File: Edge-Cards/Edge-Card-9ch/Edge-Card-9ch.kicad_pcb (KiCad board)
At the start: 2 copper layers, 20.7 x 8.8 mm, 1 part

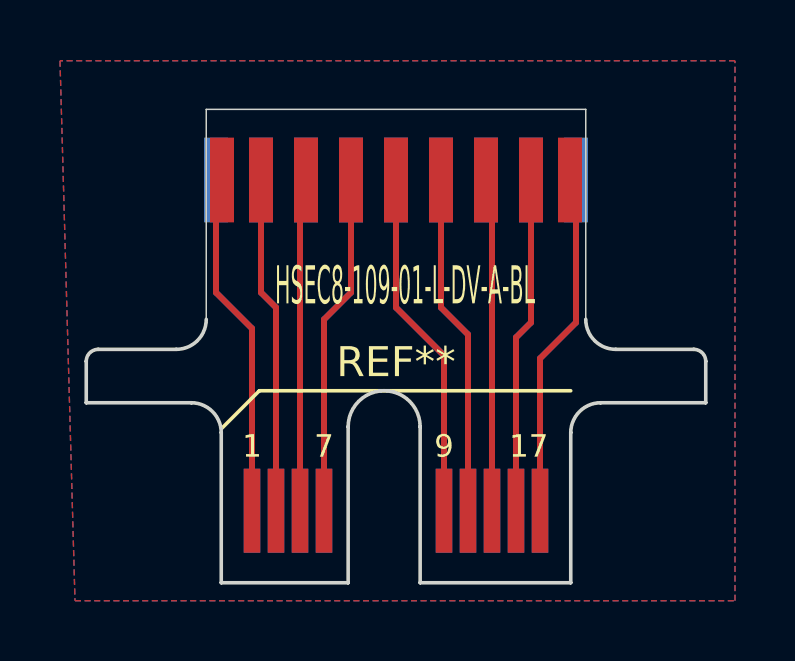
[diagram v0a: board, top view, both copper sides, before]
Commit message: Edge Card 9ch v2 + 9ch latch IV board v2 +
Updated Edge Card 9ch to v2 with expanded pads, and fixed 9ch latch IV board to reroute one trace around a hole
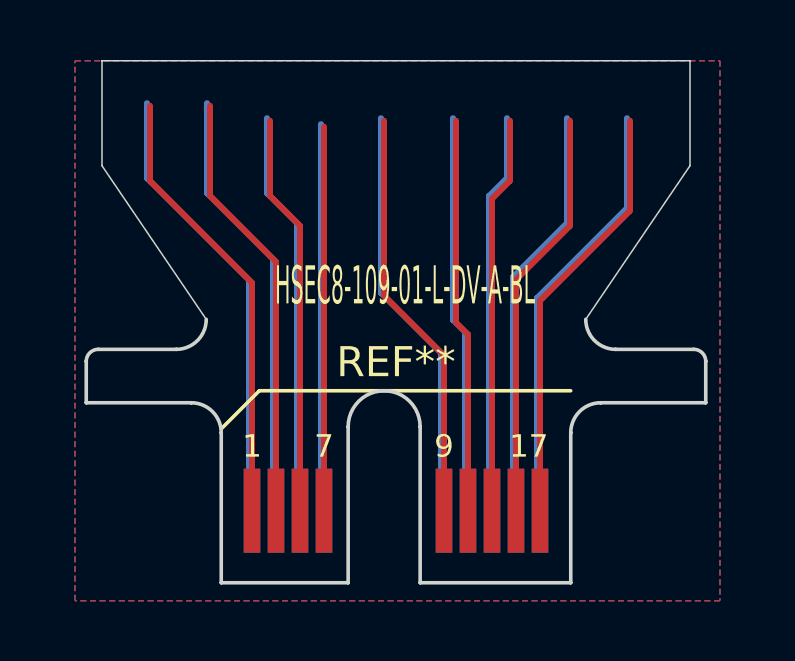
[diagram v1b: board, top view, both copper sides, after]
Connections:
- REF** pad 13: (no net) -> 13
- REF** pad 17: (no net) -> 17
- REF** pad 5: (no net) -> 5
- REF** pad 6: (no net) -> 6
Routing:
- net 1: track 21.2 -> 54.9 mm
- net 3: track 20.6 -> 0.00 mm
- net 6: track 0.00 -> 13.4 mm
- net 5: track 20.1 -> 13.4 mm
- net 13: track 20.1 -> 26.5 mm
- net 17: track 21.2 -> 26.6 mm
- net 15: track 20.6 -> 25.6 mm
- net 9: track 21.5 -> 25.8 mm
- net 11: track 20.9 -> 24.5 mm
- net 7: track 20.9 -> 23.8 mm
